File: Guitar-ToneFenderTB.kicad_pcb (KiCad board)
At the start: 2 copper layers, 53 x 35 mm, 15 parts, among them J1 Screw_Terminal_1x02, J2 Screw_Terminal_1x02, J3 Screw_Terminal_1x01

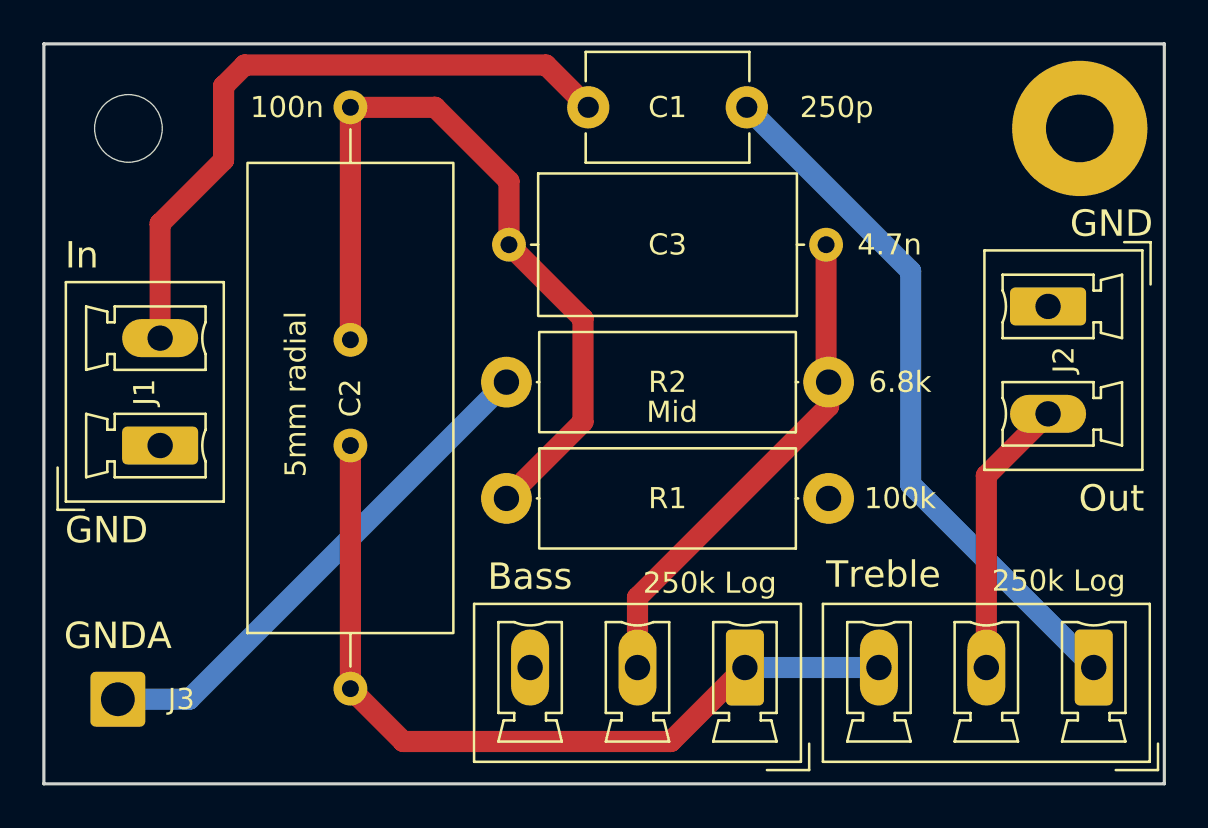
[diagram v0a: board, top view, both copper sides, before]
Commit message: Fixed error in schematic, enlarged through holes for caps.
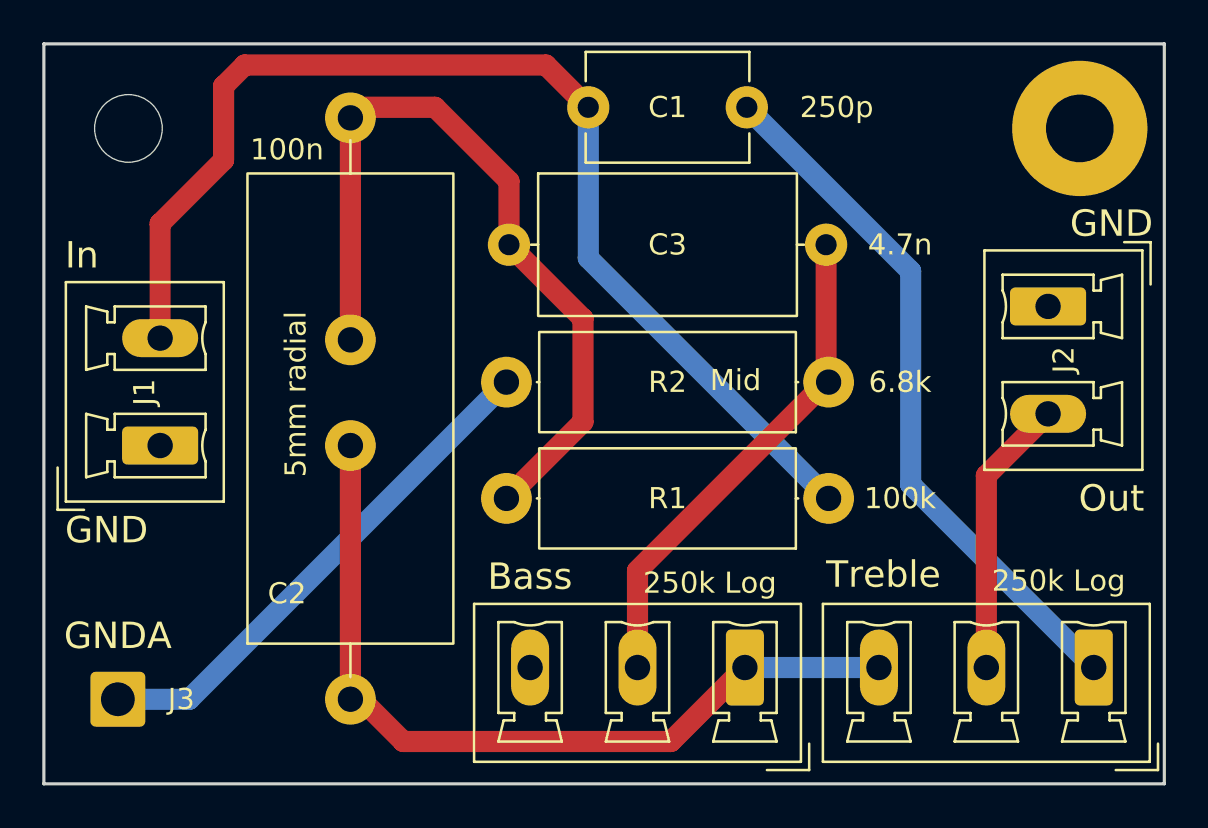
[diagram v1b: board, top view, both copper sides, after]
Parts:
- C2: footprint Capacitor_THT:C_Axial_L22.0mm_D9.5mm_P27.50mm_Horizontal -> Local:C_Axial_L22.0mm_D9.5mm_P27.50mm_Horizontal
- C3: footprint Capacitor_THT:C_Axial_L12.0mm_D6.5mm_P15.00mm_Horizontal -> Local:C_Axial_L12.0mm_D6.5mm_P15.00mm_Horizontal
- moved C2 0.50 mm to (174.5, 128.0)
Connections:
- R1 pad 1: unconnected-(R1-Pad1) -> Net-(C1-Pad1)
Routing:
- net Net-(C1-Pad1): track 31.7 -> 54.9 mm
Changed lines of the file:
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@@
 	(net 7 "Net-(C2-Pad1)")
 	(net 8 "Net-(C3-Pad2)")
-	(net 9 "unconnected-(R1-Pad1)")
 	(footprint "Connector_Phoenix_MC_HighVoltage:PhoenixContact_MCV_1,5_2-G-5.08_1x02_P5.08mm_Vertical"
 		(layer "F.Cu")
@@
 			(layers "*.Cu" "*.Mask")
 			(remove_unused_layers no)
-			(net 9 "unconnected-(R1-Pad1)")
+			(net 1 "Net-(C1-Pad1)")
 			(pintype "passive")
 		)
@@
 		)
 	)
-	(footprint "Capacitor_THT:C_Axial_L22.0mm_D9.5mm_P27.50mm_Horizontal"
+	(footprint "Local:C_Axial_L22.0mm_D9.5mm_P27.50mm_Horizontal"
 		(layer "F.Cu")
-		(at 174.5 127.5 90)
+		(at 174.5 128 90)
 		(descr "C, Axial series, Axial, Horizontal, pin pitch=27.5mm, length*diameter=22*9.5mm^2, http://cdn-reichelt.de/documents/datenblatt/B300/STYROFLEX.pdf")
 		(tags "C Axial series Axial Horizontal pin pitch 27.5mm  length 22mm diameter 9.5mm")
 		(property "Reference" "C2"
-			(at 13.75 0 90)
+			(at 5 -3 180)
 			(layer "F.SilkS")
 			(effects
@@
 		)
 		(property "Value" "100n"
-			(at 27.5 -3 180)
+			(at 26 -3 180)
 			(layer "F.SilkS")
 			(effects
@@
 		)
 		(fp_rect
-			(start -1.05 -5)
-			(end 28.55 5)
+			(start -1.55 -5)
+			(end 29.05 5)
 			(stroke
 				(width 0.05)
@@
 		(pad "1" thru_hole circle
 			(at 0 0 90)
-			(size 1.6 1.6)
-			(drill 0.8)
+			(size 2.4 2.4)
+			(drill 1.2)
 			(layers "*.Cu" "*.Mask")
 			(remove_unused_layers no)
@@
 		(pad "2" thru_hole circle
 			(at 27.5 0 90)
-			(size 1.6 1.6)
-			(drill 0.8)
+			(size 2.4 2.4)
+			(drill 1.2)
 			(layers "*.Cu" "*.Mask")
 			(remove_unused_layers no)
@@
 		(pad "1" thru_hole circle
 			(at 0 0 90)
-			(size 1.6 1.6)
-			(drill 0.8)
+			(size 2.4 2.4)
+			(drill 1.2)
 			(layers "*.Cu" "*.Mask")
 			(remove_unused_layers no)
@@
 		(pad "2" thru_hole circle
 			(at 0 0 90)
-			(size 1.6 1.6)
-			(drill 0.8)
+			(size 2.4 2.4)
+			(drill 1.2)
 			(layers "*.Cu" "*.Mask")
 			(remove_unused_layers no)
@@
 		(embedded_fonts no)
 	)
-	(footprint "Capacitor_THT:C_Axial_L12.0mm_D6.5mm_P15.00mm_Horizontal"
+	(footprint "Local:C_Axial_L12.0mm_D6.5mm_P15.00mm_Horizontal"
 		(layer "F.Cu")
 		(at 182 106.5)
@@
 		)
 		(property "Value" "4.7n"
-			(at 18 0 0)
+			(at 18.5 0 0)
 			(layer "F.SilkS")
 			(effects
@@
 		(pad "1" thru_hole circle
 			(at 0 0)
-			(size 1.6 1.6)
-			(drill 0.8)
+			(size 2 2)
+			(drill 1)
 			(layers "*.Cu" "*.Mask")
 			(remove_unused_layers no)
@@
 		(pad "2" thru_hole circle
 			(at 15 0)
-			(size 1.6 1.6)
-			(drill 0.8)
+			(size 2 2)
+			(drill 1)
 			(layers "*.Cu" "*.Mask")
 			(remove_unused_layers no)
@@
 	)
 	(gr_text "Mid"
-		(at 188.5 115 0)
+		(at 191.5 113.5 0)
 		(layer "F.SilkS")
 		(effects
@@
 		(layer "Cmts.User")
 		(pts
-			(xy 174.5 116.5) (xy 174.5 111.5)
+			(xy 174.5 116) (xy 174.5 111)
 		)
 		(height -25.5)
@@
 		)
 		(gr_text "5.0000 mm"
-			(at 147.2 114 90)
+			(at 147.2 113.5 90)
 			(layer "Cmts.User")
 			(effects
@@
 	)
 	(segment
+		(start 185.75 107.13)
+		(end 185.75 100)
+		(width 1)
+		(layer "B.Cu")
+		(net 1)
+	)
+	(segment
+		(start 197.12 118.5)
+		(end 185.75 107.13)
+		(width 1)
+		(layer "B.Cu")
+		(net 1)
+	)
+	(segment
 		(start 193.25 100)
 		(end 201 107.75)
@@
 	)
 	(segment
-		(start 188.08 123.184534)
-		(end 197.12 114.144534)
+		(start 188.08 121.92)
+		(end 197 113)
 		(width 1)
 		(layer "F.Cu")
@@
 	)
 	(segment
-		(start 197.12 114.144534)
-		(end 197.12 113)
+		(start 197 106.5)
+		(end 197 112.88)
 		(width 1)
 		(layer "F.Cu")
@@
 	)
 	(segment
-		(start 197 106.5)
-		(end 197 112.88)
+		(start 188.08 126.5)
+		(end 188.08 121.92)
 		(width 1)
 		(layer "F.Cu")
@@
 	)
 	(segment
-		(start 188.08 126.5)
-		(end 188.08 123.184534)
+		(start 197 113)
+		(end 197.12 113)
 		(width 1)
 		(layer "F.Cu")
